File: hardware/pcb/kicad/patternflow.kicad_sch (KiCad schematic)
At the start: 36 parts, among them J1 Conn_02x08_Odd_Even, J2 Screw_Terminal_01x02, J3 Screw_Terminal_01x02, SW1 RotaryEncoder_Switch, SW2 RotaryEncoder_Switch, SW3 RotaryEncoder_Switch, SW4 RotaryEncoder_Switch, U1 ESP32-S3-DevKit-44pin

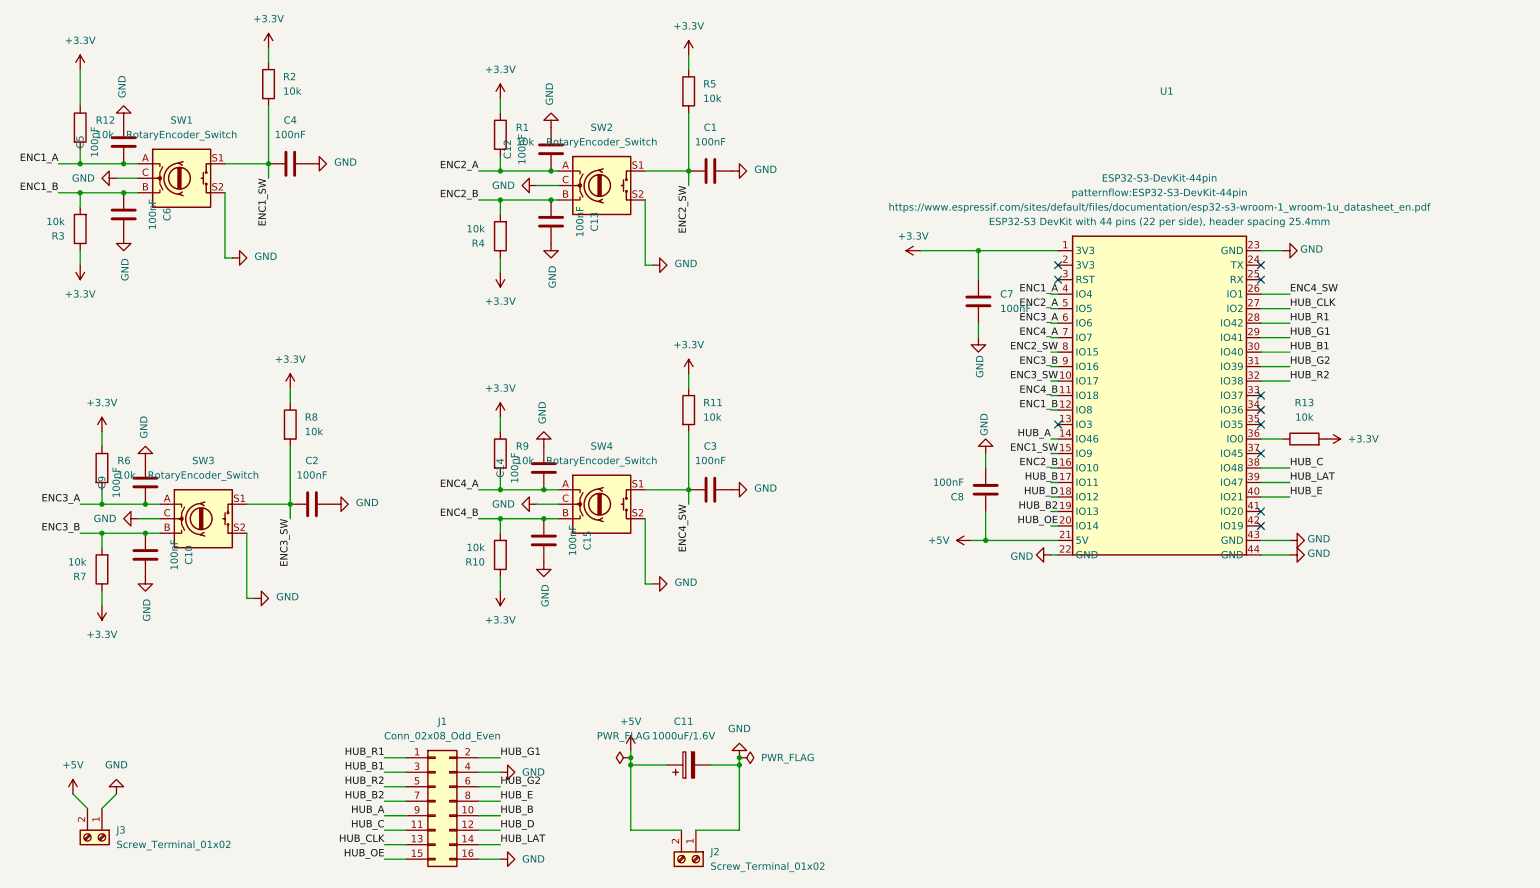
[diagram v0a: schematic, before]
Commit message: feat(hardware): rework ESP32<->J1 (HUB75) routing, regenerate v2.1 gerbers
Re-route the tangled ESP32-to-J1 area in the PCB and schematic. Pin
assignments unchanged (firmware config.h untouched). Regenerate and
overwrite the v2.1 gerber package from the updated board.

Co-Authored-By: Claude Opus 4.8 <noreply@anthropic.com>
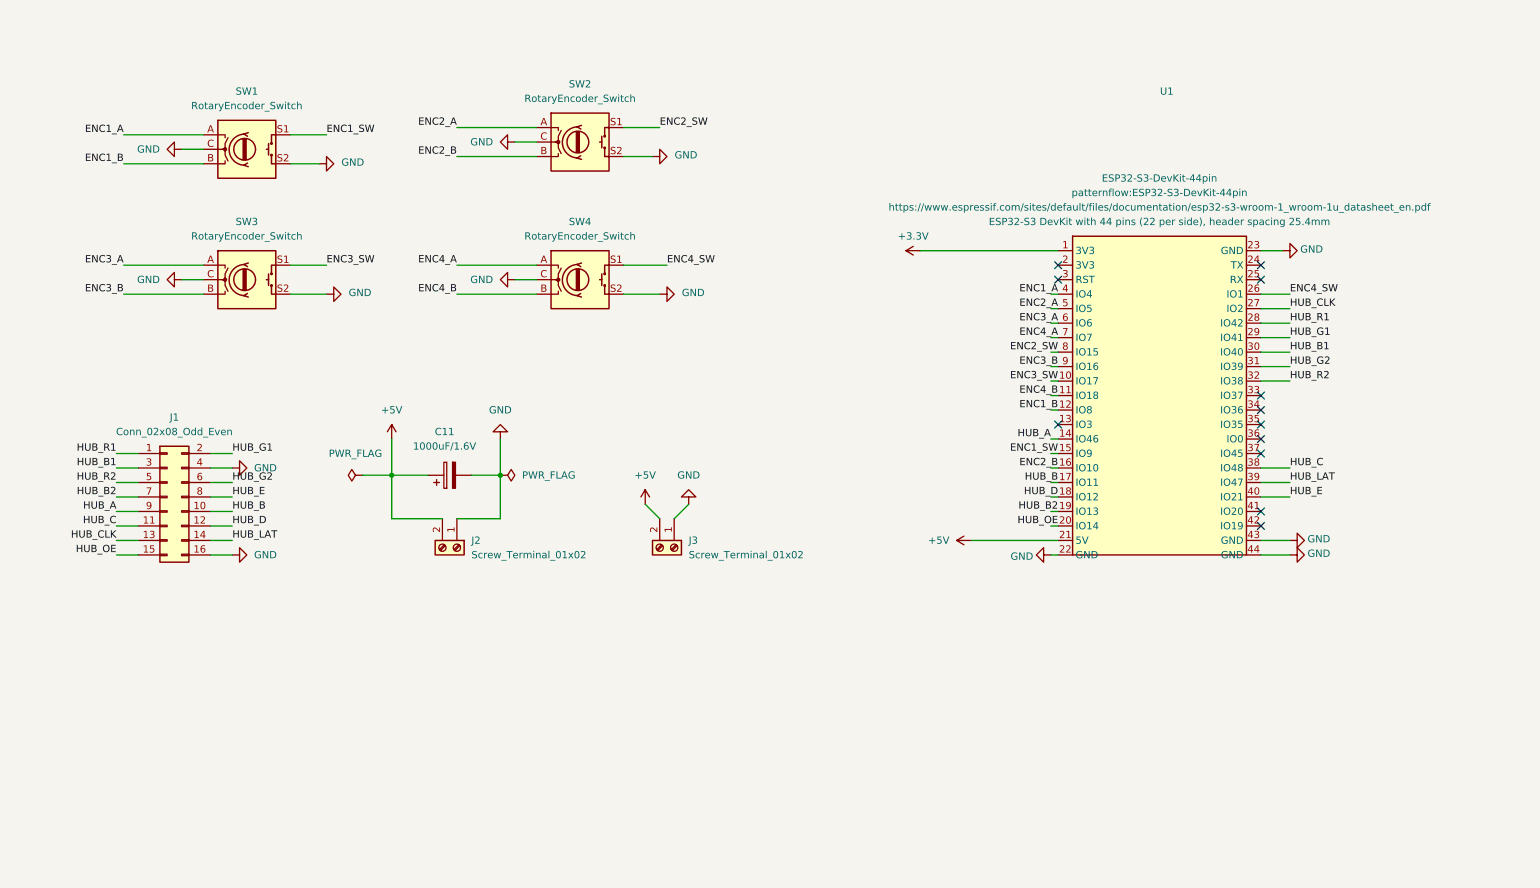
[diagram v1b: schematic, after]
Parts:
- removed C1, C10, C12, C13, C14, C15, C2, C3, C4, C5, C6, C7, C8, C9: 100nF, Capacitor_SMD:C_0805_2012Metric, symbol Device:C
- removed R1, R10, R11, R12, R2, R3, R4, R5, R6, R7, R8, R9: 10k, Resistor_SMD:R_0805_2012Metric, symbol Device:R
- removed R13: 10k, symbol Device:R
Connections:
- no-connect marks 11 -> 12
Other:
- moved on the sheet: C11, J1, J2, J3, SW1, SW2, SW3, SW4

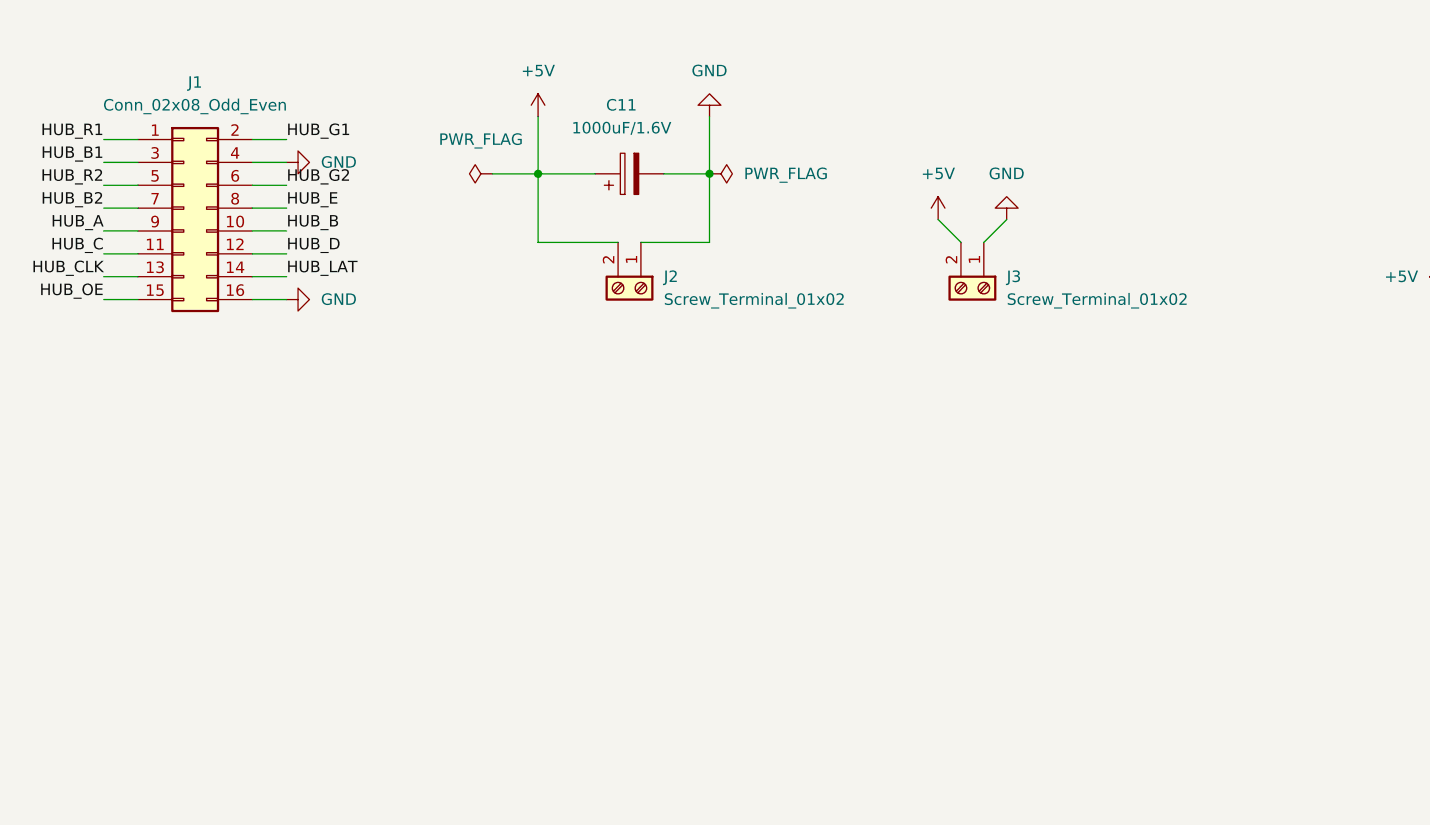
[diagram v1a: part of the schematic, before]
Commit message: feat(pcb): v2.2 USB Type-C power input, SMD-free board
Rework the board per the power-supply change in #114:
- Switch power input to USB Type-C (SHOU HAN TYPE-C 14P CC-2.6,
  LCSC C5187475); add its footprint and 3D models.
- Remove all SMD passives; the two 5.1k USB-C CC pull-downs are
  hand-soldered, so the whole board is hand-solderable.
- Move the Type-C connector toward center for easier cable insertion.
- Reduce overall board size; bump silkscreen to v2.2.

Generate fab output patternflow_v2.2_test_gerber.zip (DRC clean: 0
violations / 0 unconnected). The _test suffix stays until a fabricated
board is verified.

Refs #114

Co-Authored-By: Claude Opus 4.8 <noreply@anthropic.com>
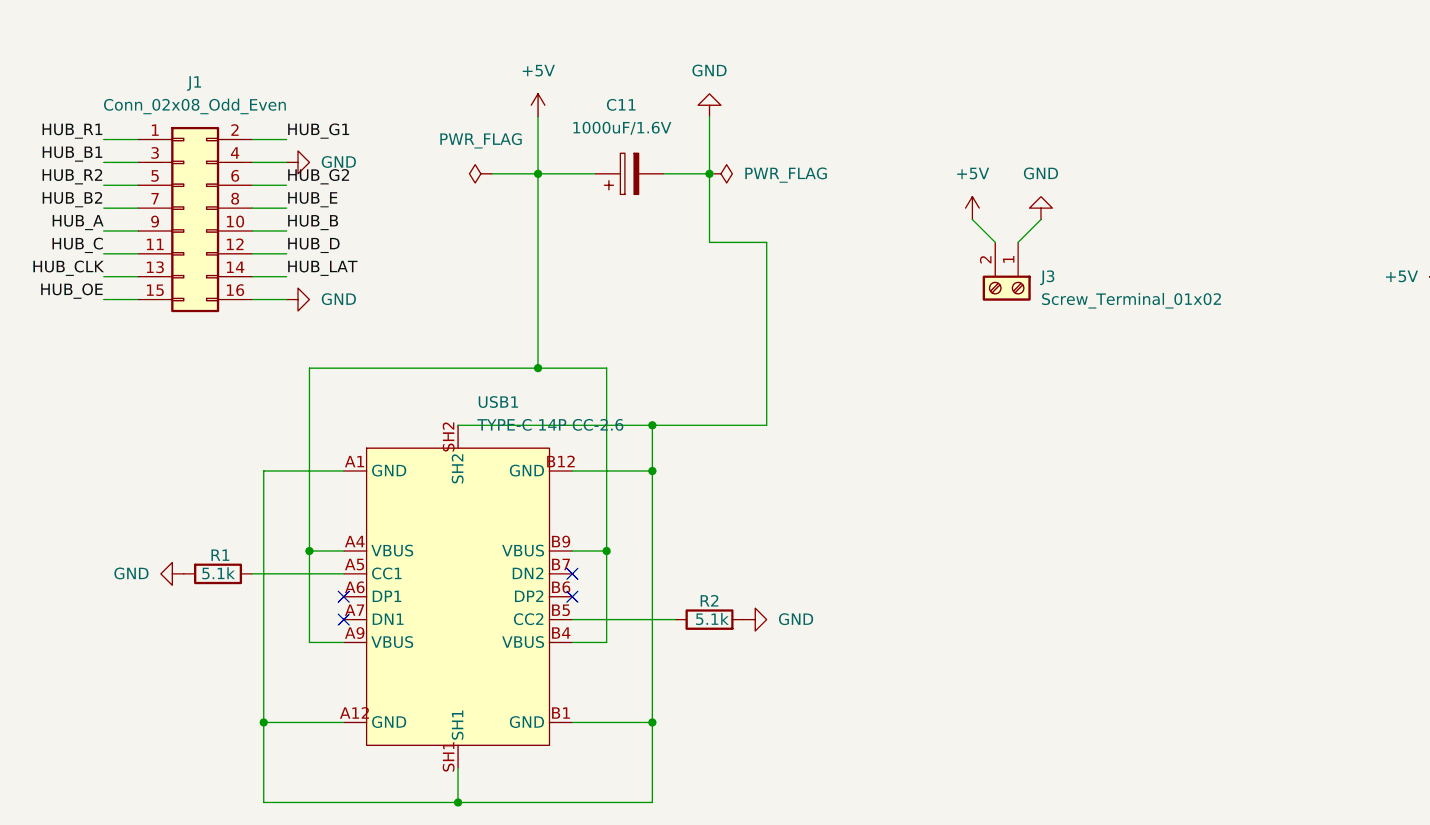
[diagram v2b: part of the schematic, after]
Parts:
- removed J2: Screw_Terminal_01x02, TerminalBlock:TerminalBlock_MaiXu_MX126-5.0-02P_1x02_P5.00mm, symbol Connector:Screw_Terminal_01x02
- added R1, R2: 5.1k, Resistor_THT:R_Axial_DIN0207_L6.3mm_D2.5mm_P7.62mm_Horizontal, symbol Device:R
- added USB1: TYPE-C 14P CC-2.6, patternflow:TYPE-C-TH_TYPE-C-14P-CC-2.6, symbol patternflow:TYPE-C14PCC-2.6
- SW1, SW2, SW3, SW4: footprint Rotary_Encoder:RotaryEncoder_Alps_EC12E-Switch_Vertical_H20mm -> Rotary_Encoder:RotaryEncoder_Bourns_Vertical_PEC12R-3x17F-Sxxxx
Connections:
- net +5V: now also USB1.A4 (VBUS), USB1.A9 (VBUS), USB1.B4 (VBUS), USB1.B9 (VBUS)
- net GND: now also R1.2, R2.2, USB1.A1 (GND), USB1.A12 (GND), USB1.B1 (GND), USB1.B12 (GND), USB1.SH1, USB1.SH2
- new net: R1.1, USB1.A5 (CC1)
- new net: R2.1, USB1.B5 (CC2)
- no-connect marks 12 -> 16
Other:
- moved on the sheet: J3
